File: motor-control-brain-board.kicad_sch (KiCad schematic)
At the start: 35 parts, among them J1 GPIO, J10 PWM, J11 PWR, J12 POWER_SENSE, J13 MISC_SENSE, J2 I2C, J3 SERIAL_1, J4 SERIAL_2, J5 CAN, J6 SPI, J7 USB_C_Receptacle_USB2.0_16P, J8 SWD, J9 POS_SENSE, SW1 RST, U1 TLV76750QWDRBxQ1, U2 TLV76733QWDRBxQ1

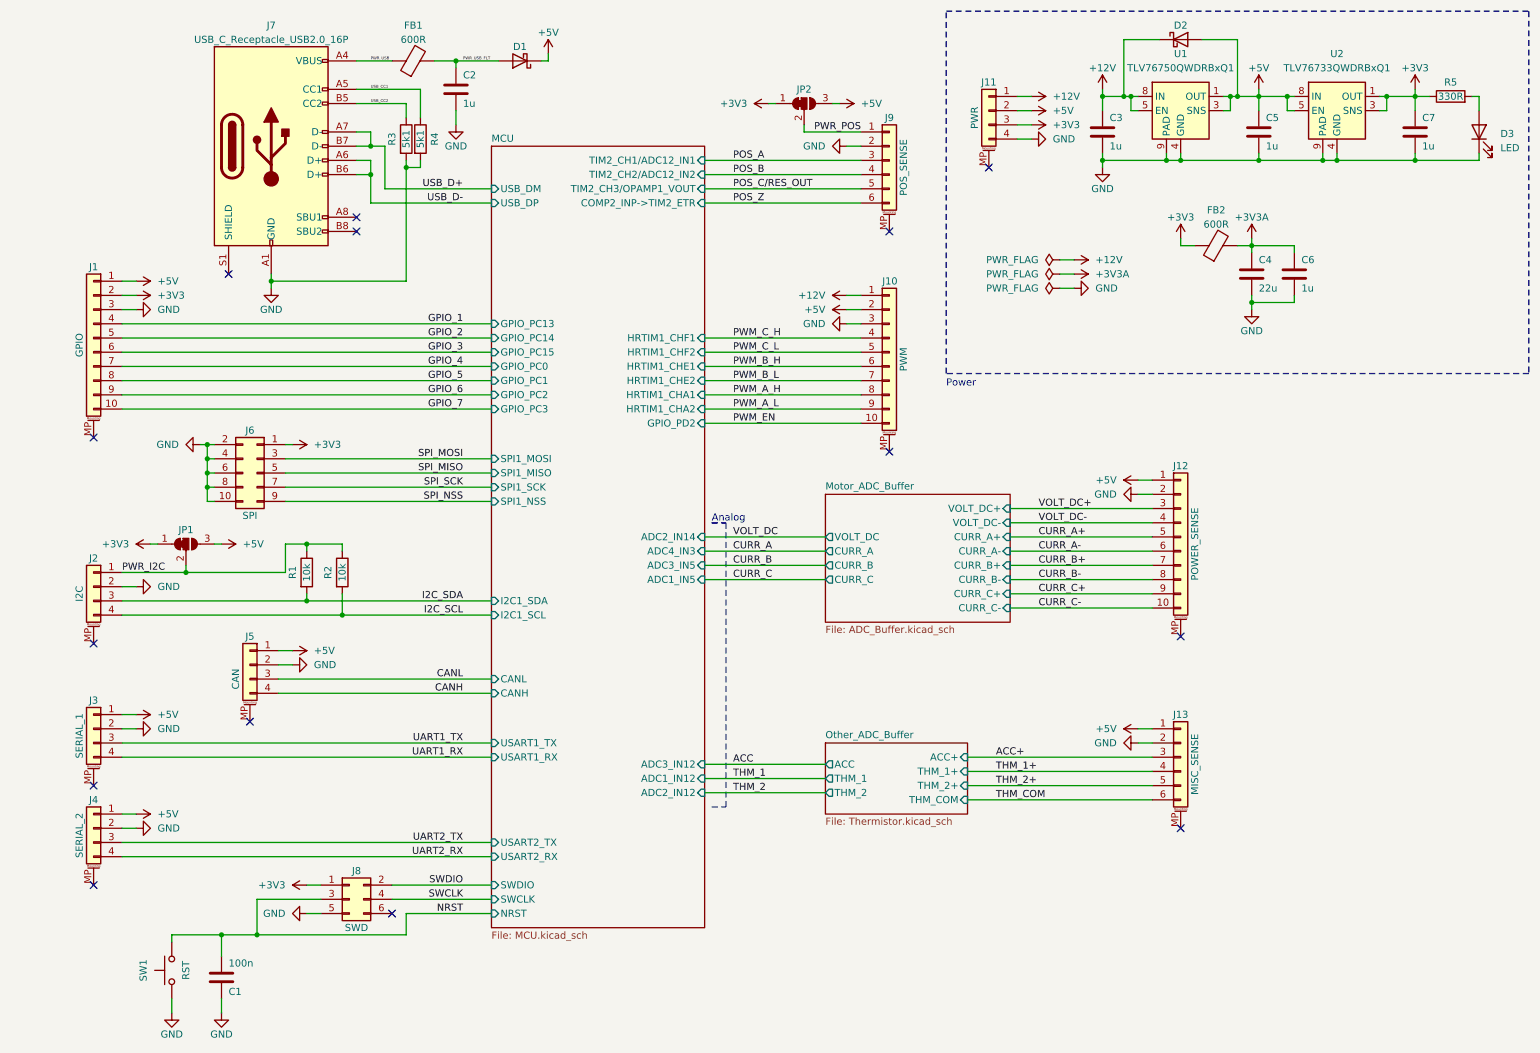
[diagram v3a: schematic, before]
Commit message: Changed to LPUART for 1 channel to improve routing etc. Can now add 1 more ADC as needed. Todo: Figure out GPIO and add oscillator
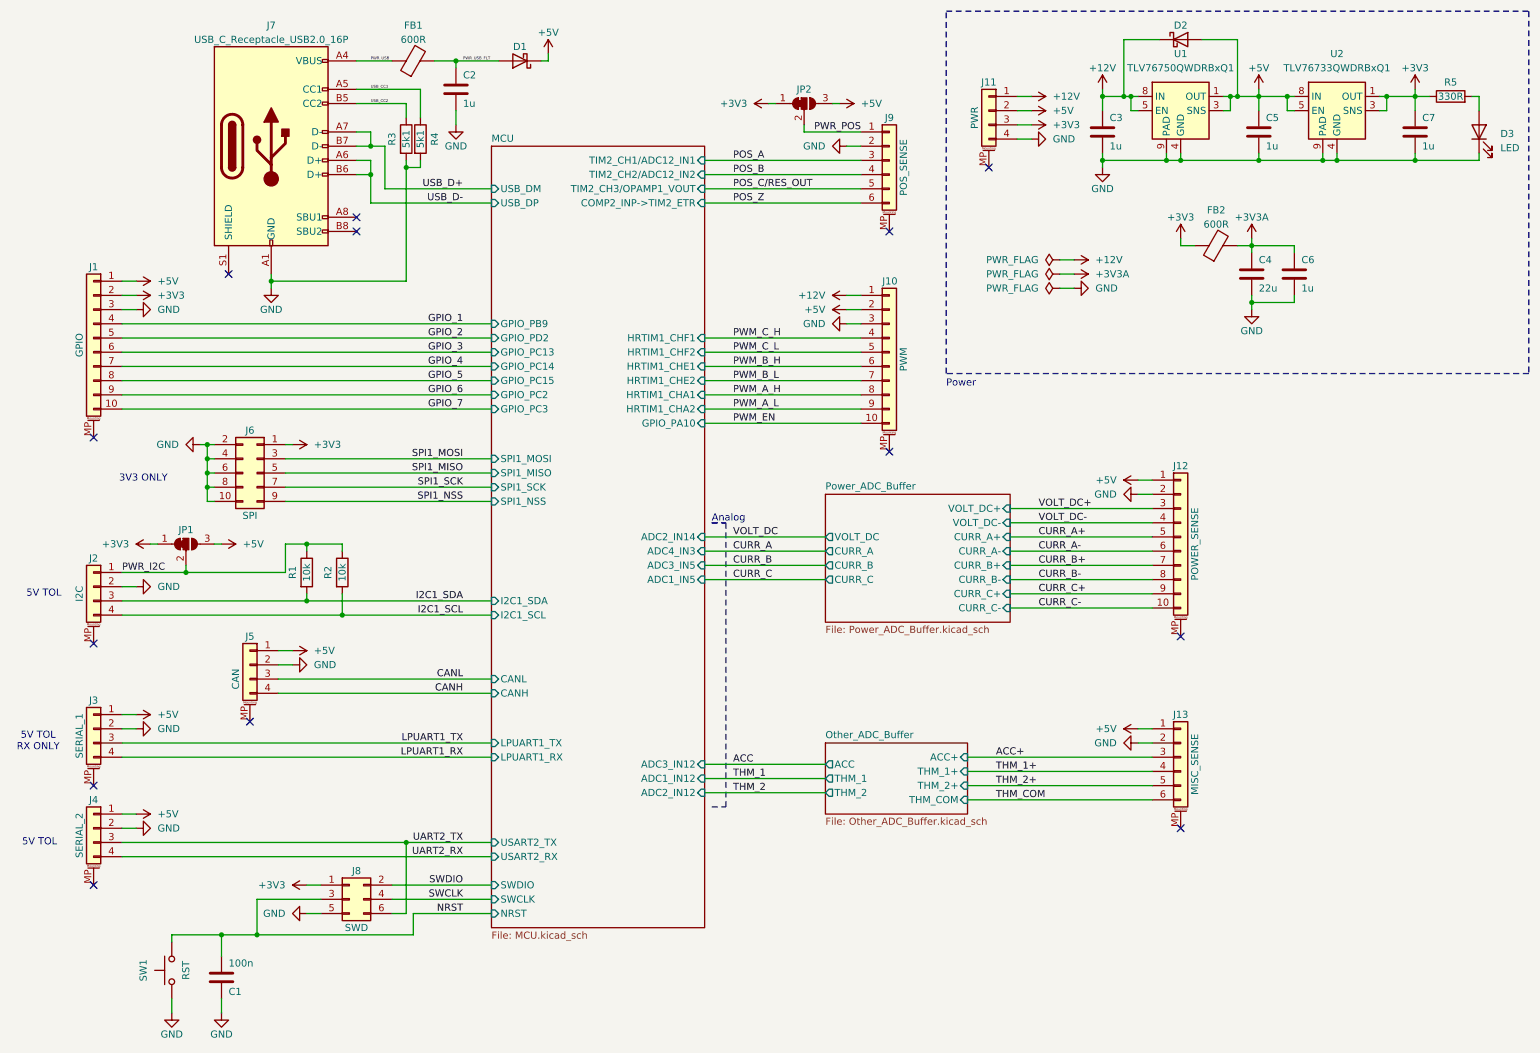
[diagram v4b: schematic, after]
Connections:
- net UART2_TX: now also J8.6 (Pin_6)
- net I2C_SCL renamed I2C1_SCL
- net I2C_SDA renamed I2C1_SDA
- net SPI_MISO renamed SPI1_MISO
- net SPI_MOSI renamed SPI1_MOSI
- net SPI_NSS renamed SPI1_NSS
- net SPI_SCK renamed SPI1_SCK
- net UART1_RX renamed LPUART1_RX
- net UART1_TX renamed LPUART1_TX
- no-connect marks 14 -> 13
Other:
- sheet Motor_ADC_Buffer renamed Power_ADC_Buffer
- sheet MCU ports: added GPIO_PA10, GPIO_PB9, LPUART1_RX, LPUART1_TX; removed GPIO_PC0, GPIO_PC1, USART1_RX, USART1_TX
- sheet Other_ADC_Buffer: file Thermistor.kicad_sch -> Other_ADC_Buffer.kicad_sch
- sheet Power_ADC_Buffer: file ADC_Buffer.kicad_sch -> Power_ADC_Buffer.kicad_sch
- note added: "3V3 ONLY"
- note added: "5V TOL"
- note added: "5V TOL RX ONLY"
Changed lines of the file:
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@@
 		)
 	)
+	(text "5V TOL\nRX ONLY"
+		(exclude_from_sim no)
+		(at 18.034 143.256 0)
+		(effects
+			(font
+				(size 1.27 1.27)
+			)
+		)
+	)
 	(text "Analog"
 		(exclude_from_sim no)
@@
 		)
 	)
+	(text "3V3 ONLY"
+		(exclude_from_sim no)
+		(at 36.83 96.266 0)
+		(effects
+			(font
+				(size 1.27 1.27)
+			)
+		)
+	)
 	(text "Power"
 		(exclude_from_sim no)
@@
 		)
 	)
+	(text "5V TOL"
+		(exclude_from_sim no)
+		(at 19.05 116.84 0)
+		(effects
+			(font
+				(size 1.27 1.27)
+			)
+		)
+	)
+	(text "5V TOL"
+		(exclude_from_sim no)
+		(at 18.288 161.29 0)
+		(effects
+			(font
+				(size 1.27 1.27)
+			)
+		)
+	)
 	(junction
 		(at 57.15 177.8)
@@
 	)
 	(junction
+		(at 83.82 161.29)
+		(diameter 0)
+		(color 0 0 0 0)
+	)
+	(junction
 		(at 92.71 21.59)
 		(diameter 0)
@@
 	)
 	(no_connect
-		(at 81.28 173.99)
-	)
-	(no_connect
 		(at 170.18 91.44)
 	)
@@
 	(wire
 		(pts
+			(xy 83.82 161.29) (xy 99.06 161.29)
+		)
+		(stroke
+			(width 0)
+			(type default)
+		)
+	)
+	(wire
+		(pts
 			(xy 83.82 60.96) (xy 59.69 60.96)
 		)
@@
 	(wire
 		(pts
-			(xy 57.15 177.8) (xy 83.82 177.8)
+			(xy 57.15 177.8) (xy 85.09 177.8)
 		)
 		(stroke
@@
 	(wire
 		(pts
-			(xy 83.82 177.8) (xy 83.82 173.99)
+			(xy 85.09 177.8) (xy 85.09 173.99)
 		)
 		(stroke
@@
 	(wire
 		(pts
+			(xy 83.82 161.29) (xy 83.82 173.99)
+		)
+		(stroke
+			(width 0)
+			(type default)
+		)
+	)
+	(wire
+		(pts
 			(xy 81.28 171.45) (xy 99.06 171.45)
 		)
@@
 	(wire
 		(pts
-			(xy 33.02 161.29) (xy 99.06 161.29)
+			(xy 33.02 161.29) (xy 83.82 161.29)
 		)
 		(stroke
@@
 	(wire
 		(pts
+			(xy 81.28 173.99) (xy 83.82 173.99)
+		)
+		(stroke
+			(width 0)
+			(type default)
+		)
+	)
+	(wire
+		(pts
 			(xy 33.02 71.12) (xy 99.06 71.12)
 		)
@@
 	(wire
 		(pts
-			(xy 83.82 173.99) (xy 99.06 173.99)
+			(xy 85.09 173.99) (xy 99.06 173.99)
 		)
 		(stroke
@@
 		)
 	)
-	(label "SPI_MOSI"
+	(label "SPI1_MOSI"
 		(at 93.98 92.71 180)
 		(effects
@@
 		)
 	)
-	(label "UART1_TX"
+	(label "LPUART1_TX"
 		(at 93.98 143.51 180)
 		(effects
@@
 		)
 	)
-	(label "SPI_NSS"
+	(label "SPI1_NSS"
 		(at 93.98 100.33 180)
 		(effects
@@
 		)
 	)
-	(label "SPI_MISO"
+	(label "SPI1_MISO"
 		(at 93.98 95.25 180)
 		(effects
@@
 		)
 	)
-	(label "SPI_SCK"
+	(label "SPI1_SCK"
 		(at 93.98 97.79 180)
 		(effects
@@
 		)
 	)
-	(label "I2C_SCL"
+	(label "I2C1_SCL"
 		(at 93.98 120.65 180)
 		(effects
@@
 		)
 	)
-	(label "I2C_SDA"
+	(label "I2C1_SDA"
 		(at 93.98 118.11 180)
 		(effects
@@
 		)
 	)
-	(label "UART1_RX"
+	(label "LPUART1_RX"
 		(at 93.98 146.05 180)
 		(effects
@@
 			)
 		)
-		(pin "GPIO_PD2" input
-			(at 137.16 86.36 0)
-			(effects
-				(font
-					(size 1.27 1.27)
-				)
-				(justify right)
-			)
-		)
-		(pin "GPIO_PC15" input
-			(at 99.06 73.66 180)
-			(effects
-				(font
-					(size 1.27 1.27)
-				)
-				(justify left)
-			)
-		)
-		(pin "GPIO_PC14" input
-			(at 99.06 71.12 180)
-			(effects
-				(font
-					(size 1.27 1.27)
-				)
-				(justify left)
-			)
-		)
-		(pin "GPIO_PC13" input
-			(at 99.06 68.58 180)
-			(effects
-				(font
-					(size 1.27 1.27)
-				)
-				(justify left)
-			)
-		)
-		(pin "GPIO_PC1" input
-			(at 99.06 78.74 180)
-			(effects
-				(font
-					(size 1.27 1.27)
-				)
-				(justify left)
-			)
-		)
 		(pin "GPIO_PC2" input
 			(at 99.06 81.28 180)
@@
 			)
 		)
-		(pin "GPIO_PC0" input
-			(at 99.06 76.2 180)
-			(effects
-				(font
-					(size 1.27 1.27)
-				)
-				(justify left)
-			)
-		)
 		(pin "USB_DM" input
 			(at 99.06 44.45 180)
@@
 			)
 		)
-		(pin "USART1_TX" input
-			(at 99.06 143.51 180)
-			(effects
-				(font
-					(size 1.27 1.27)
-				)
-				(justify left)
-			)
-		)
-		(pin "USART1_RX" input
-			(at 99.06 146.05 180)
-			(effects
-				(font
-					(size 1.27 1.27)
-				)
-				(justify left)
-			)
-		)
 		(pin "USART2_RX" input
 			(at 99.06 163.83 180)
@@
 			)
 		)
+		(pin "LPUART1_RX" input
+			(at 99.06 146.05 180)
+			(effects
+				(font
+					(size 1.27 1.27)
+				)
+				(justify left)
+			)
+		)
+		(pin "LPUART1_TX" input
+			(at 99.06 143.51 180)
+			(effects
+				(font
+					(size 1.27 1.27)
+				)
+				(justify left)
+			)
+		)
+		(pin "GPIO_PC15" input
+			(at 99.06 78.74 180)
+			(effects
+				(font
+					(size 1.27 1.27)
+				)
+				(justify left)
+			)
+		)
+		(pin "GPIO_PC14" input
+			(at 99.06 76.2 180)
+			(effects
+				(font
+					(size 1.27 1.27)
+				)
+				(justify left)
+			)
+		)
+		(pin "GPIO_PC13" input
+			(at 99.06 73.66 180)
+			(effects
+				(font
+					(size 1.27 1.27)
+				)
+				(justify left)
+			)
+		)
+		(pin "GPIO_PA10" input
+			(at 137.16 86.36 0)
+			(effects
+				(font
+					(size 1.27 1.27)
+				)
+				(justify right)
+			)
+		)
+		(pin "GPIO_PD2" input
+			(at 99.06 71.12 180)
+			(effects
+				(font
+					(size 1.27 1.27)
+				)
+				(justify left)
+			)
+		)
+		(pin "GPIO_PB9" input
+			(at 99.06 68.58 180)
+			(effects
+				(font
+					(size 1.27 1.27)
+				)
+				(justify left)
+			)
+		)
 		(instances
 			(project "motor-control-brain-board"
@@
 			)
 		)
-		(property "Sheetfile" "Thermistor.kicad_sch"
+		(property "Sheetfile" "Other_ADC_Buffer.kicad_sch"
 			(at 158.75 156.7946 0)
 			(effects
@@
 			(color 0 0 0 0.0000)
 		)
-		(property "Sheetname" "Motor_ADC_Buffer"
+		(property "Sheetname" "Power_ADC_Buffer"
 			(at 158.75 98.3484 0)
 			(effects
@@
 			)
 		)
-		(property "Sheetfile" "ADC_Buffer.kicad_sch"
+		(property "Sheetfile" "Power_ADC_Buffer.kicad_sch"
 			(at 158.75 122.5046 0)
 			(effects

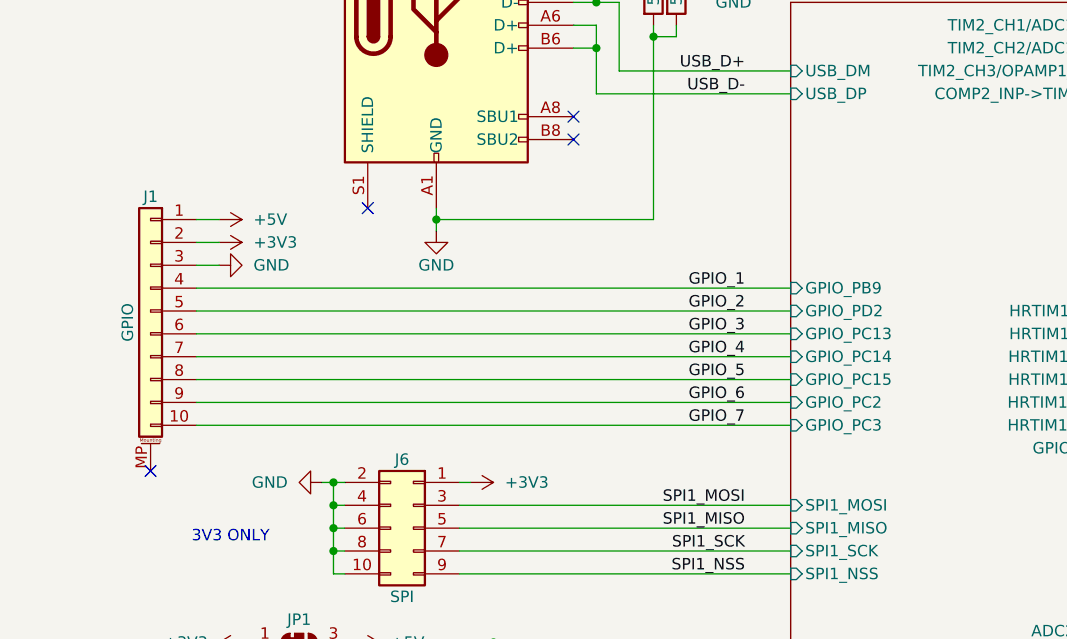
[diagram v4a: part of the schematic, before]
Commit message: Figured out GPIO and added oscillator to schematic, need to pick part
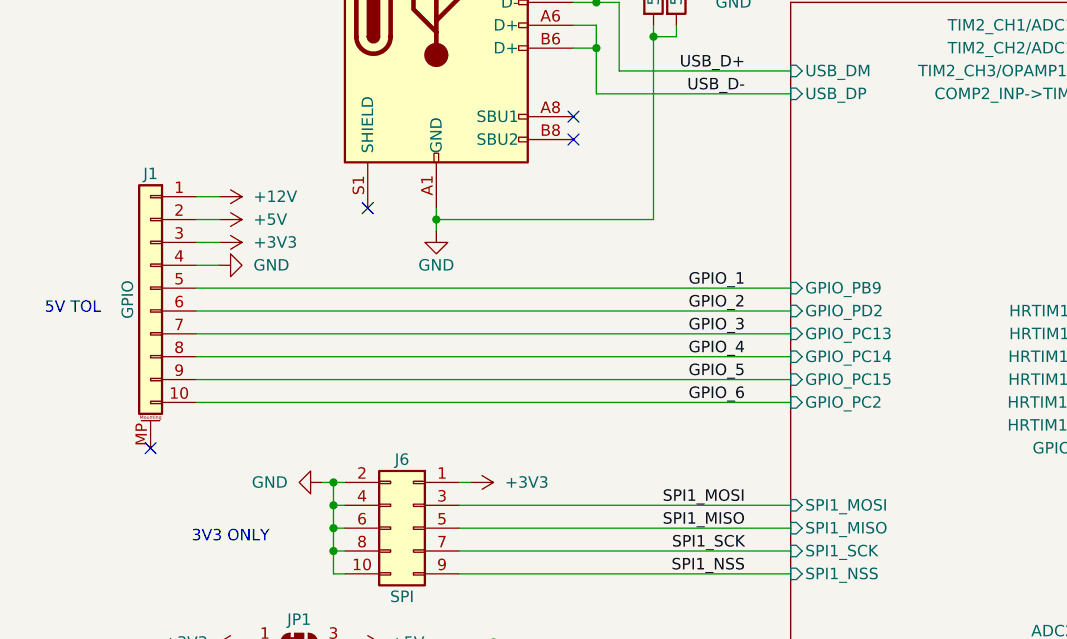
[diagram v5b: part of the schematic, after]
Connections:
- net GPIO_7 is gone; now on net GPIO_6: J1.10 (Pin_10)
- net +12V: now also J1.1 (Pin_1)
- net +3V3: now also J1.3 (Pin_3); no longer J1.2 (Pin_2)
- net +5V: now also J1.2 (Pin_2); no longer J1.1 (Pin_1)
- net GND: now also J1.4 (Pin_4); no longer J1.3 (Pin_3)
- net GPIO_1: now also J1.5 (Pin_5); no longer J1.4 (Pin_4)
- net GPIO_2: now also J1.6 (Pin_6); no longer J1.5 (Pin_5)
- net GPIO_3: now also J1.7 (Pin_7); no longer J1.6 (Pin_6)
- net GPIO_4: now also J1.8 (Pin_8); no longer J1.7 (Pin_7)
- net GPIO_5: now also J1.9 (Pin_9); no longer J1.8 (Pin_8)
- net GPIO_6: no longer J1.9 (Pin_9)
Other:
- sheet MCU ports: added none; removed GPIO_PC3
- moved on the sheet: J1
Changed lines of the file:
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@@
 	(text "5V TOL"
 		(exclude_from_sim no)
+		(at 19.304 70.866 0)
+		(effects
+			(font
+				(size 1.27 1.27)
+			)
+		)
+	)
+	(text "5V TOL"
+		(exclude_from_sim no)
 		(at 18.288 161.29 0)
 		(effects
@@
 	)
 	(no_connect
-		(at 27.94 88.9)
+		(at 27.94 86.36)
 	)
 	(no_connect
@@
 		)
 	)
+	(wire
+		(pts
+			(xy 35.56 58.42) (xy 33.02 58.42)
+		)
+		(stroke
+			(width 0)
+			(type default)
+		)
+	)
 	(polyline
 		(pts
@@
 	(wire
 		(pts
-			(xy 33.02 83.82) (xy 99.06 83.82)
-		)
-		(stroke
-			(width 0)
-			(type default)
-		)
-	)
-	(wire
-		(pts
 			(xy 33.02 78.74) (xy 99.06 78.74)
 		)
@@
 		)
 	)
-	(label "GPIO_7"
-		(at 93.98 83.82 180)
-		(effects
-			(font
-				(size 1.27 1.27)
-			)
-			(justify right bottom)
-		)
-	)
 	(label "USB_CC2"
 		(at 77.47 29.21 0)
@@
 	(symbol
 		(lib_id "Connector_Generic_MountingPin:Conn_01x10_MountingPin")
-		(at 27.94 71.12 0)
+		(at 27.94 68.58 0)
 		(mirror y)
 		(unit 1)
@@
 		(dnp no)
 		(property "Reference" "J1"
-			(at 27.94 58.42 0)
+			(at 27.94 55.88 0)
 			(effects
 				(font
@@
 		)
 		(property "Value" "GPIO"
-			(at 25.4 72.39 90)
+			(at 25.4 69.85 90)
 			(effects
 				(font
@@
 		)
 		(property "Footprint" "Connector_JST:JST_GH_SM10B-GHS-TB_1x10-1MP_P1.25mm_Horizontal"
-			(at 27.94 71.12 0)
+			(at 27.94 68.58 0)
 			(effects
 				(font
@@
 		)
 		(property "Datasheet" "~"
-			(at 27.94 71.12 0)
+			(at 27.94 68.58 0)
 			(effects
 				(font
@@
 		)
 		(property "Description" "Generic connectable mounting pin connector, single row, 01x10, script generated (kicad-library-utils/schlib/autogen/connector/)"
-			(at 27.94 71.12 0)
+			(at 27.94 68.58 0)
 			(effects
 				(font
@@
 	)
 	(symbol
+		(lib_id "power:+12V")
+		(at 35.56 58.42 270)
+		(unit 1)
+		(exclude_from_sim no)
+		(in_bom yes)
+		(on_board yes)
+		(dnp no)
+		(property "Reference" "#PWR0100"
+			(at 31.75 58.42 0)
+			(effects
+				(font
+					(size 1.27 1.27)
+				)
+				(hide yes)
+			)
+		)
+		(property "Value" "+12V"
+			(at 39.37 58.42 90)
+			(effects
+				(font
+					(size 1.27 1.27)
+				)
+				(justify left)
+			)
+		)
+		(property "Footprint" ""
+			(at 35.56 58.42 0)
+			(effects
+				(font
+					(size 1.27 1.27)
+				)
+				(hide yes)
+			)
+		)
+		(property "Datasheet" ""
+			(at 35.56 58.42 0)
+			(effects
+				(font
+					(size 1.27 1.27)
+				)
+				(hide yes)
+			)
+		)
+		(property "Description" "Power symbol creates a global label with name \"+12V\""
+			(at 35.56 58.42 0)
+			(effects
+				(font
+					(size 1.27 1.27)
+				)
+				(hide yes)
+			)
+		)
+		(pin "1"
+		)
+		(instances
+			(project "motor-control-brain-board"
+				(path "/7261d109-8405-40e9-921c-d95f374a7164"
+					(reference "#PWR0100")
+					(unit 1)
+				)
+			)
+		)
+	)
+	(symbol
 		(lib_id "power:+3V3")
 		(at 195.58 33.02 270)
@@
 			(effects
 				(font
-					(size 1.27 1.27)
-				)
-				(justify left)
-			)
-		)
-		(pin "GPIO_PC3" input
-			(at 99.06 83.82 180)
-			(effects
-				(font

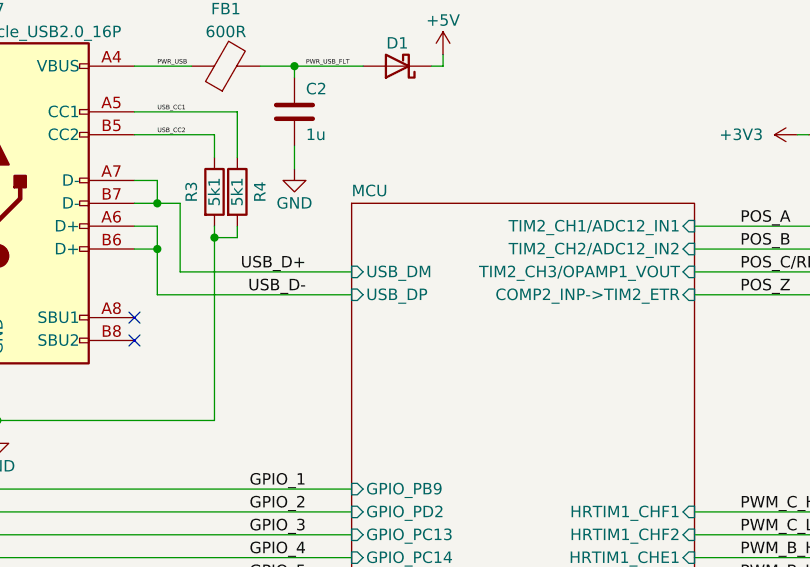
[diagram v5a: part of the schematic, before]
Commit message: Moved MCU to make more room for routing, updated crystal package/PN
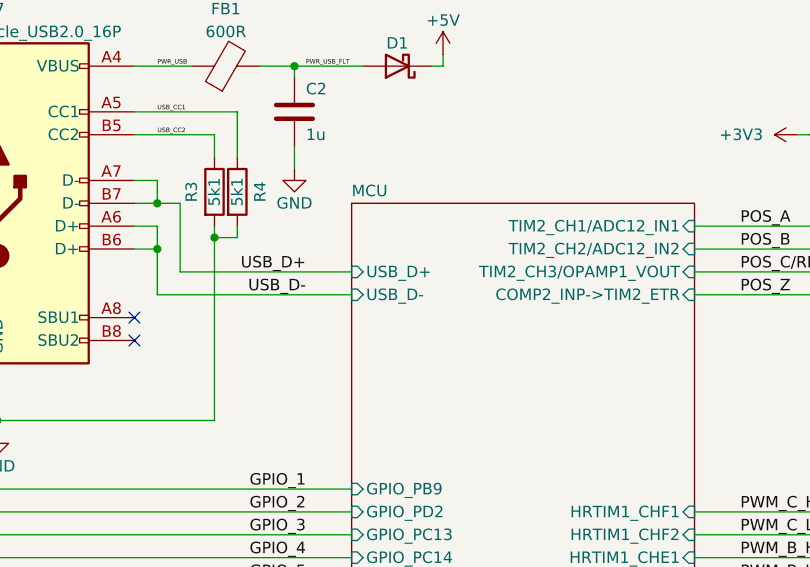
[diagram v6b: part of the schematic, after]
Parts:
- J6: footprint User_Connector:Samtec_FTSH-105-XX-X-DV-K -> Connector_PinHeader_1.27mm:PinHeader_2x05_P1.27mm_Vertical
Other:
- sheet MCU ports: added USB_D+, USB_D-; removed USB_DM, USB_DP
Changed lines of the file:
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@@
 			)
 		)
-		(property "Footprint" "User_Connector:Samtec_FTSH-105-XX-X-DV-K"
+		(property "Footprint" "Connector_PinHeader_1.27mm:PinHeader_2x05_P1.27mm_Vertical"
 			(at 57.15 95.25 0)
 			(effects
@@
 			)
 		)
-		(pin "USB_DM" input
-			(at 99.06 44.45 180)
-			(effects
-				(font
-					(size 1.27 1.27)
-				)
-				(justify left)
-			)
-		)
 		(pin "SPI1_NSS" input
 			(at 99.06 100.33 180)
@@
 			)
 		)
-		(pin "USB_DP" input
-			(at 99.06 46.99 180)
-			(effects
-				(font
-					(size 1.27 1.27)
-				)
-				(justify left)
-			)
-		)
 		(pin "TIM2_CH3{slash}OPAMP1_VOUT" input
 			(at 137.16 44.45 0)
@@
 			(effects
 				(font
+					(size 1.27 1.27)
+				)
+				(justify left)
+			)
+		)
+		(pin "USB_D+" input
+			(at 99.06 44.45 180)
+			(effects
+				(font
+					(size 1.27 1.27)
+				)
+				(justify left)
+			)
+		)
+		(pin "USB_D-" input
+			(at 99.06 46.99 180)
+			(effects
+				(font
